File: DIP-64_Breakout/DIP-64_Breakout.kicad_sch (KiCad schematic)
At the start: 6 parts, among them J1 DIP-64 Socket, J2 Left, J3 Right, J4 Decoupling Capacitor, J5 +5V In, J6 GND In

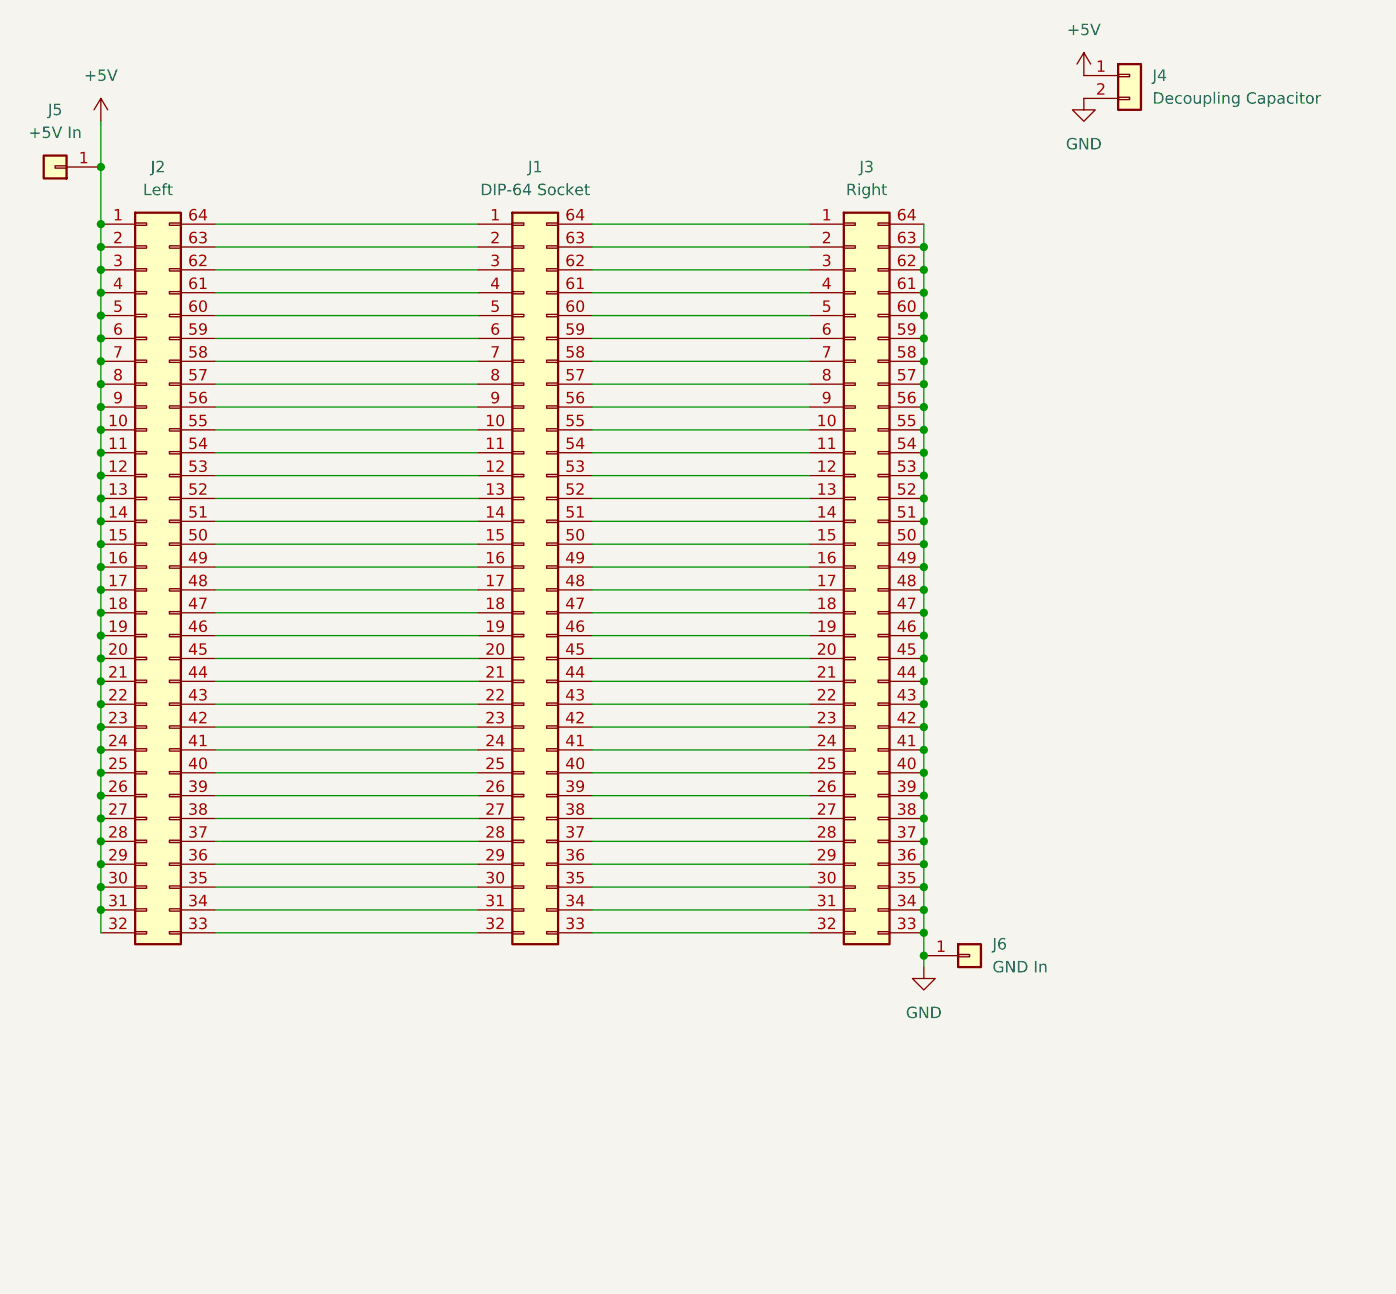
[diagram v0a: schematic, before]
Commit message: Modified power input pins
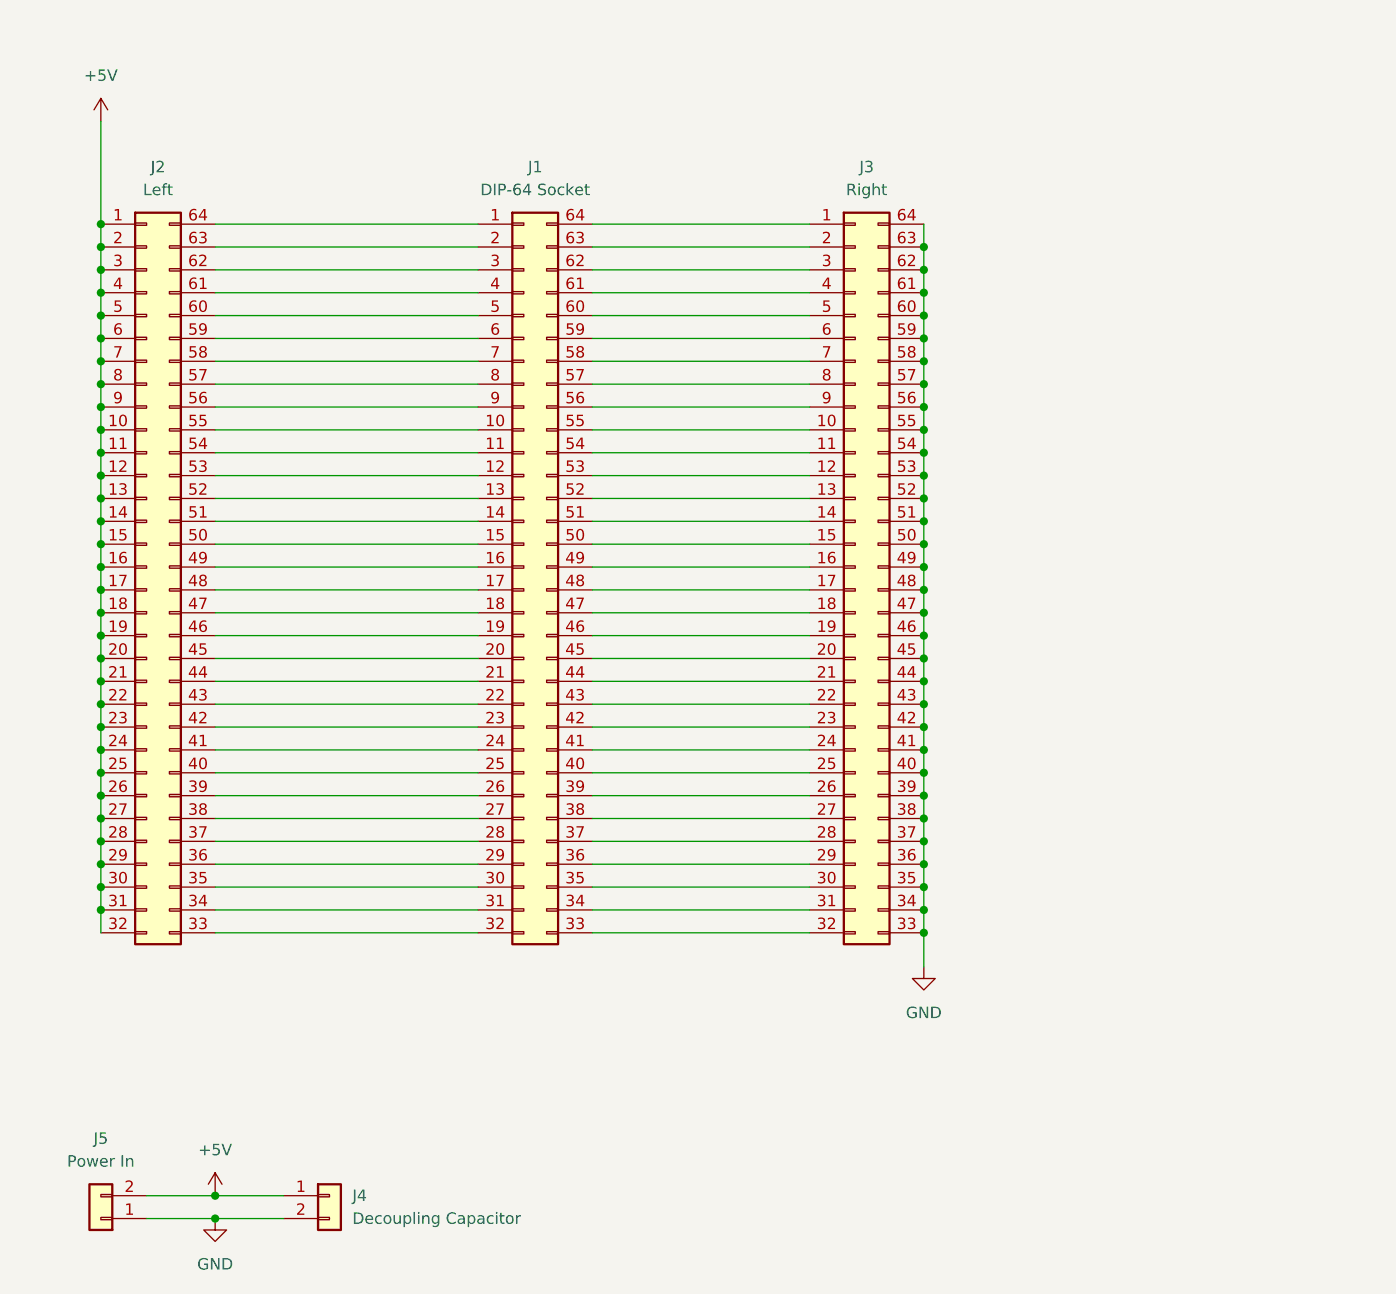
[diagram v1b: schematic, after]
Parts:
- removed J5: +5V In, Connector_PinHeader_2.54mm:PinHeader_1x01_P2.54mm_Vertical, symbol Connector_Generic:Conn_01x01
- removed J6: GND In, Connector_PinHeader_2.54mm:PinHeader_1x01_P2.54mm_Vertical, symbol Connector_Generic:Conn_01x01
- added J5: Power In, Connector_PinHeader_2.54mm:PinHeader_1x02_P2.54mm_Vertical, symbol Connector_Generic:Conn_01x02
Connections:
- net +5V: now also J5.2 (Pin_2)
- net GND: now also J5.1 (Pin_1)
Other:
- moved on the sheet: J4
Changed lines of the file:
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@@
 	(title_block
 		(title "Breakout for 1.27mm Pitch DIP-64")
-		(date "4/JUL/2026")
+		(date "5/JUL/2026")
 		(rev "A")
 		(company "Brett Hallen")
@@
 	)
 	(junction
-		(at 189.23 139.7)
-		(diameter 0)
-		(color 0 0 0 0)
-	)
-	(junction
 		(at 97.79 96.52)
 		(diameter 0)
@@
 	)
 	(junction
+		(at 110.49 166.37)
+		(diameter 0)
+		(color 0 0 0 0)
+	)
+	(junction
 		(at 97.79 99.06)
 		(diameter 0)
@@
 	)
 	(junction
-		(at 97.79 52.07)
-		(diameter 0)
-		(color 0 0 0 0)
-	)
-	(junction
 		(at 189.23 104.14)
 		(diameter 0)
@@
 	)
 	(junction
+		(at 110.49 168.91)
+		(diameter 0)
+		(color 0 0 0 0)
+	)
+	(junction
 		(at 189.23 132.08)
 		(diameter 0)
@@
 	(wire
 		(pts
+			(xy 102.87 168.91) (xy 110.49 168.91)
+		)
+		(stroke
+			(width 0)
+			(type default)
+		)
+	)
+	(wire
+		(pts
 			(xy 176.53 71.12) (xy 152.4 71.12)
 		)
@@
 	(wire
 		(pts
-			(xy 189.23 139.7) (xy 189.23 137.16)
+			(xy 189.23 137.16) (xy 189.23 140.97)
 		)
 		(stroke
@@
 	(wire
 		(pts
-			(xy 97.79 52.07) (xy 97.79 58.42)
+			(xy 97.79 46.99) (xy 97.79 58.42)
 		)
 		(stroke
@@
 	(wire
 		(pts
+			(xy 110.49 166.37) (xy 118.11 166.37)
+		)
+		(stroke
+			(width 0)
+			(type default)
+		)
+	)
+	(wire
+		(pts
 			(xy 97.79 127) (xy 97.79 129.54)
 		)
@@
 	(wire
 		(pts
-			(xy 97.79 46.99) (xy 97.79 52.07)
-		)
-		(stroke
-			(width 0)
-			(type default)
-		)
-	)
-	(wire
-		(pts
 			(xy 189.23 124.46) (xy 189.23 127)
 		)
@@
 	(wire
 		(pts
+			(xy 110.49 168.91) (xy 118.11 168.91)
+		)
+		(stroke
+			(width 0)
+			(type default)
+		)
+	)
+	(wire
+		(pts
 			(xy 176.53 106.68) (xy 152.4 106.68)
 		)
@@
 	(wire
 		(pts
-			(xy 189.23 140.97) (xy 189.23 139.7)
-		)
-		(stroke
-			(width 0)
-			(type default)
-		)
-	)
-	(wire
-		(pts
 			(xy 110.49 132.08) (xy 139.7 132.08)
 		)
@@
 		(pts
 			(xy 176.53 88.9) (xy 152.4 88.9)
+		)
+		(stroke
+			(width 0)
+			(type default)
+		)
+	)
+	(wire
+		(pts
+			(xy 102.87 166.37) (xy 110.49 166.37)
 		)
 		(stroke
@@
 	(symbol
 		(lib_id "power:GND")
-		(at 207.01 44.45 0)
+		(at 110.49 168.91 0)
 		(unit 1)
 		(body_style 1)
@@
 		(fields_autoplaced yes)
 		(property "Reference" "#PWR04"
-			(at 207.01 50.8 0)
+			(at 110.49 175.26 0)
 			(hide yes)
 			(show_name no)
@@
 		)
 		(property "Value" "GND"
-			(at 207.01 49.53 0)
+			(at 110.49 173.99 0)
 			(show_name no)
 			(do_not_autoplace no)
@@
 		)
 		(property "Footprint" ""
-			(at 207.01 44.45 0)
+			(at 110.49 168.91 0)
 			(hide yes)
 			(show_name no)
@@
 		)
 		(property "Datasheet" ""
-			(at 207.01 44.45 0)
+			(at 110.49 168.91 0)
 			(hide yes)
 			(show_name no)
@@
 		)
 		(property "Description" "Power symbol creates a global label with name \"GND\" , ground"
-			(at 207.01 44.45 0)
+			(at 110.49 168.91 0)
 			(hide yes)
 			(show_name no)
@@
 	(symbol
 		(lib_id "Connector_Generic:Conn_01x02")
-		(at 212.09 41.91 0)
+		(at 123.19 166.37 0)
 		(unit 1)
 		(body_style 1)
@@
 		(fields_autoplaced yes)
 		(property "Reference" "J4"
-			(at 214.63 41.9099 0)
+			(at 125.73 166.3699 0)
 			(show_name no)
 			(do_not_autoplace no)
@@
 		)
 		(property "Value" "Decoupling Capacitor"
-			(at 214.63 44.4499 0)
+			(at 125.73 168.9099 0)
 			(show_name no)
 			(do_not_autoplace no)
@@
 		)
 		(property "Footprint" "Connector_PinHeader_2.54mm:PinHeader_1x02_P2.54mm_Vertical"
-			(at 212.09 41.91 0)
+			(at 123.19 166.37 0)
 			(hide yes)
 			(show_name no)
@@
 		)
 		(property "Datasheet" ""
-			(at 212.09 41.91 0)
+			(at 123.19 166.37 0)
 			(hide yes)
 			(show_name no)
@@
 		)
 		(property "Description" "Generic connector, single row, 01x02, script generated (kicad-library-utils/schlib/autogen/connector/)"
-			(at 212.09 41.91 0)
+			(at 123.19 166.37 0)
 			(hide yes)
 			(show_name no)
@@
 	(symbol
 		(lib_id "power:+5V")
-		(at 207.01 41.91 0)
+		(at 110.49 166.37 0)
 		(unit 1)
 		(body_style 1)
@@
 		(fields_autoplaced yes)
 		(property "Reference" "#PWR03"
-			(at 207.01 45.72 0)
+			(at 110.49 170.18 0)
 			(hide yes)
 			(show_name no)
@@
 		)
 		(property "Value" "+5V"
-			(at 207.01 36.83 0)
+			(at 110.49 161.29 0)
 			(show_name no)
 			(do_not_autoplace no)
@@
 		)
 		(property "Footprint" ""
-			(at 207.01 41.91 0)
+			(at 110.49 166.37 0)
 			(hide yes)
 			(show_name no)
@@
 		)
 		(property "Datasheet" ""
-			(at 207.01 41.91 0)
+			(at 110.49 166.37 0)
 			(hide yes)
 			(show_name no)
@@
 		)
 		(property "Description" "Power symbol creates a global label with name \"+5V\""
-			(at 207.01 41.91 0)
+			(at 110.49 166.37 0)
 			(hide yes)
 			(show_name no)
@@
 	)
 	(symbol
-		(lib_id "Connector_Generic:Conn_01x01")
-		(at 92.71 52.07 180)
+		(lib_id "Connector_Generic:Conn_01x02")
+		(at 97.79 168.91 180)
 		(unit 1)
 		(body_style 1)
@@
 		(fields_autoplaced yes)
 		(property "Reference" "J5"
-			(at 92.71 45.72 0)
-			(show_name no)
-			(do_not_autoplace no)
-			(effects
-				(font
-					(size 1.27 1.27)
-				)
-			)
-		)
-		(property "Value" "+5V In"
-			(at 92.71 48.26 0)
-			(show_name no)
-			(do_not_autoplace no)
-			(effects
-				(font
-					(size 1.27 1.27)
-				)
-			)
-		)
-		(property "Footprint" "Connector_PinHeader_2.54mm:PinHeader_1x01_P2.54mm_Vertical"
-			(at 92.71 52.07 0)
+			(at 97.79 160.02 0)
+			(show_name no)
+			(do_not_autoplace no)
+			(effects
+				(font
+					(size 1.27 1.27)
+				)
+			)
+		)
+		(property "Value" "Power In"
+			(at 97.79 162.56 0)
+			(show_name no)
+			(do_not_autoplace no)
+			(effects
+				(font
+					(size 1.27 1.27)
+				)
+			)
+		)
+		(property "Footprint" "Connector_PinHeader_2.54mm:PinHeader_1x02_P2.54mm_Vertical"
+			(at 97.79 168.91 0)
 			(hide yes)
 			(show_name no)
@@
 		)
 		(property "Datasheet" ""
-			(at 92.71 52.07 0)
-			(hide yes)
-			(show_name no)
-			(do_not_autoplace no)
-			(effects
-				(font
-					(size 1.27 1.27)
-				)
-			)
-		)
-		(property "Description" "Generic connector, single row, 01x01, script generated (kicad-library-utils/schlib/autogen/connector/)"
-			(at 92.71 52.07 0)
+			(at 97.79 168.91 0)
+			(hide yes)
+			(show_name no)
+			(do_not_autoplace no)
+			(effects
+				(font
+					(size 1.27 1.27)
+				)
+			)
+		)
+		(property "Description" "Generic connector, single row, 01x02, script generated (kicad-library-utils/schlib/autogen/connector/)"
+			(at 97.79 168.91 0)
 			(hide yes)
 			(show_name no)
@@
 		)
 		(pin "1"
+		)
+		(pin "2"
 		)
 		(instances
@@
 					(unit 1)
 				)
-			)
-		)
-	)
-	(symbol
-		(lib_id "Connector_Generic:Conn_01x01")
-		(at 194.31 139.7 0)
-		(unit 1)
-		(body_style 1)
-		(exclude_from_sim no)
-		(in_bom yes)
-		(on_board yes)
-		(in_pos_files yes)
-		(dnp no)
-		(fields_autoplaced yes)
-		(property "Reference" "J6"
-			(at 196.85 138.4299 0)
-			(show_name no)
-			(do_not_autoplace no)
-			(effects
-				(font
-					(size 1.27 1.27)
-				)
-				(justify left)
-			)
-		)
-		(property "Value" "GND In"
-			(at 196.85 140.9699 0)
-			(show_name no)
-			(do_not_autoplace no)
-			(effects
-				(font
-					(size 1.27 1.27)
-				)
-				(justify left)
-			)
-		)
-		(property "Footprint" "Connector_PinHeader_2.54mm:PinHeader_1x01_P2.54mm_Vertical"
-			(at 194.31 139.7 0)
-			(hide yes)
-			(show_name no)
-			(do_not_autoplace no)
-			(effects
-				(font
-					(size 1.27 1.27)
-				)
-			)
-		)
-		(property "Datasheet" ""
-			(at 194.31 139.7 0)
-			(hide yes)
-			(show_name no)
-			(do_not_autoplace no)
-			(effects
-				(font
-					(size 1.27 1.27)
-				)
-			)
-		)
-		(property "Description" "Generic connector, single row, 01x01, script generated (kicad-library-utils/schlib/autogen/connector/)"
-			(at 194.31 139.7 0)
-			(hide yes)
-			(show_name no)
-			(do_not_autoplace no)
-			(effects
-				(font
-					(size 1.27 1.27)
-				)
-			)
-		)
-		(pin "1"
-		)
-		(instances
-			(project "DIP-64_Breakout"
-				(path "/915fba1b-5ce2-4565-a678-31d348b16f67"
-					(reference "J6")
-					(unit 1)
-				)
